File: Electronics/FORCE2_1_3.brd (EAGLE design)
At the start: 148.7 x 33.1 mm, 17 parts, among them J4 PTH, SW1 22-23-2031, SW2 22-23-2031, X1 22-23-2051, X2 22-23-2051, X3 22-23-2021

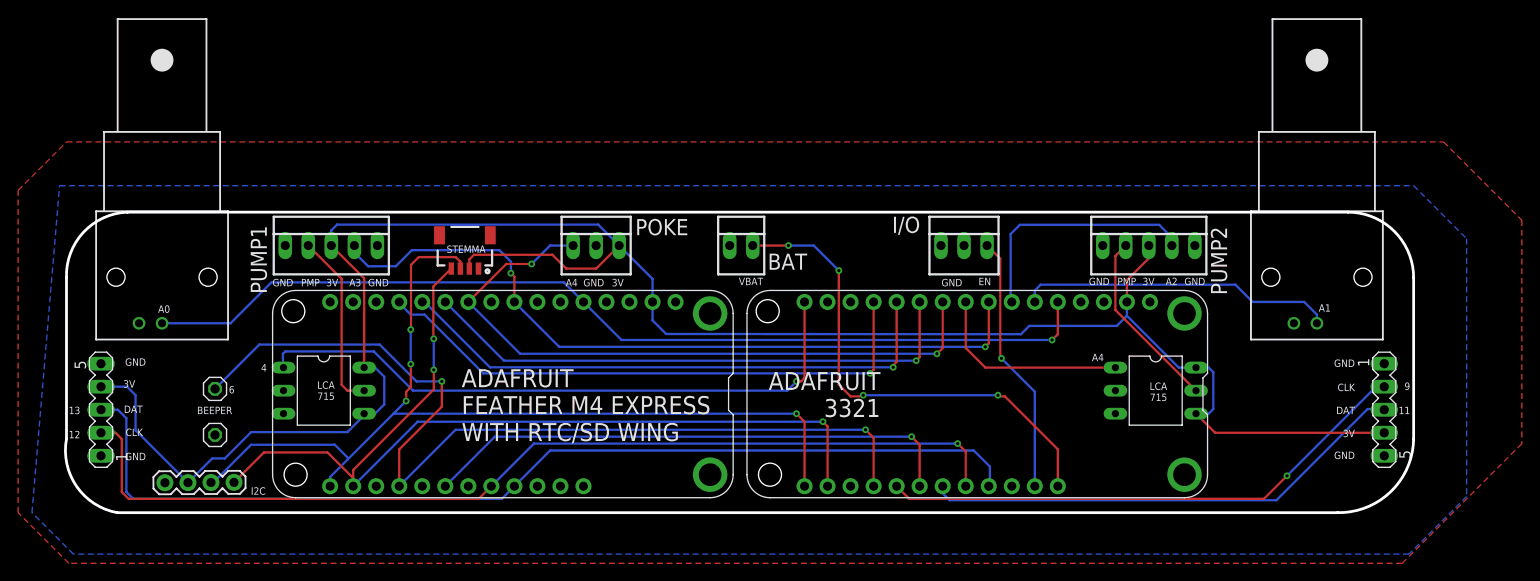
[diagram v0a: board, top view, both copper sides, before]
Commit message: First commit. Added electronics, stl file, and readme
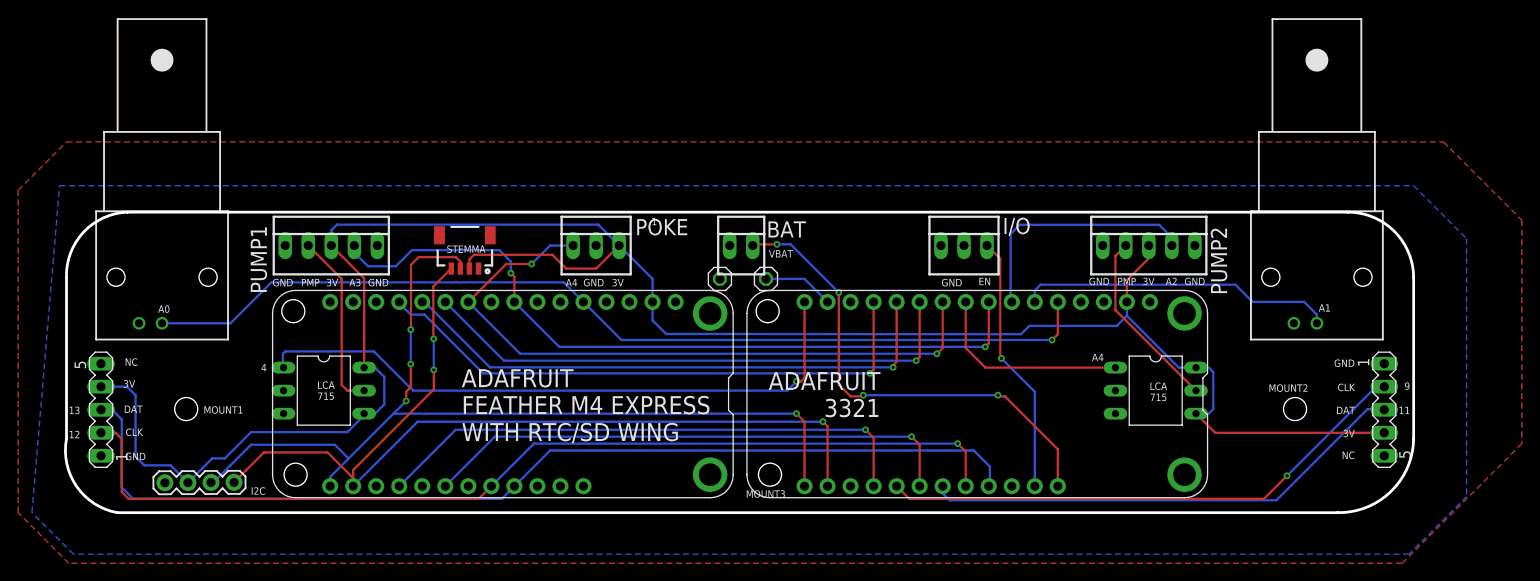
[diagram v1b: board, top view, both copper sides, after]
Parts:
- moved BEEP1 62.0 mm to (76.6, 27.1)
- moved GND 58.3 mm to (71.6, 27.1), turned to 270 degrees
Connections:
- net 1: now also BEEP1.1
- net 6: no longer BEEP1.1
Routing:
- net 6: track 102.8 -> 60.6 mm, vias 2 -> 1
- net 1: track 0.00 -> 7.85 mm
- net 3V: track 228.5 -> 230.2 mm
- net VBAT: track 54.5 -> 53.2 mm
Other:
- board text added: "1"
- board text added: "Designed by Alex Legaria v1.3 OCT2022"
- board text added: "MOUNT1"
- board text added: "MOUNT2"
- board text added: "MOUNT3"
- board text added: "NC"
- board text removed: "6"
- board text removed: "Designed by Alex Legaria v1.2 SEP2022"
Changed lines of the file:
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@@
 <drawing>
 <settings>
-<setting alwaysvectorfont="yes"/>
+<setting alwaysvectorfont="no"/>
 <setting verticaltext="up"/>
 </settings>
@@
 <wire x1="-0.508" y1="9.398" x2="-0.508" y2="27.178" width="0.3048" layer="20"/>
 <wire x1="-0.508" y1="27.178" x2="6.223" y2="34.417" width="0.3048" layer="20" curve="-90"/>
-<text x="76.835" y="28.067" size="1.778" layer="25">BAT</text>
-<text x="90.551" y="32.131" size="1.778" layer="25">I/O</text>
+<text x="76.708" y="31.623" size="1.778" layer="25">BAT</text>
+<text x="102.743" y="32.004" size="1.778" layer="25">I/O</text>
 <text x="62.23" y="31.877" size="1.778" layer="25">POKE</text>
 <text x="127.508" y="25.273" size="1.778" layer="25" rot="R90">PUMP2</text>
@@
 <text x="113.919" y="18.796" size="0.8128" layer="25" rot="R180">A4</text>
 <text x="7.076784375" y="15.875" size="0.8128" layer="25" rot="R180">3V</text>
-<text x="8.255" y="18.288" size="0.8128" layer="25" rot="R180">GND</text>
+<text x="7.366" y="18.288" size="0.8128" layer="25" rot="R180">NC</text>
 <text x="7.92474375" y="10.541" size="0.8128" layer="25" rot="R180">CLK</text>
 <text x="7.897965625" y="13.081" size="0.8128" layer="25" rot="R180">DAT</text>
 <text x="8.255" y="7.874" size="0.8128" layer="25" rot="R180">GND</text>
-<text x="141.605" y="8.001" size="0.8128" layer="25" rot="R180">GND</text>
+<text x="141.605" y="8.001" size="0.8128" layer="25" rot="R180">NC</text>
 <text x="21.59" y="17.653" size="0.8128" layer="25" rot="R180">4</text>
 <text x="27.432" y="27.051" size="0.8128" layer="25" rot="R180">PMP</text>
@@
 <text x="98.298" y="27.051" size="0.8128" layer="25" rot="R180">GND</text>
 <text x="101.473" y="27.178" size="0.8128" layer="25" rot="R180">EN</text>
-<text x="76.327" y="27.178" size="0.8128" layer="25" rot="R180">VBAT</text>
+<text x="79.629" y="30.226" size="0.8128" layer="25" rot="R180">VBAT</text>
 <text x="1.016" y="10.287" size="0.8128" layer="25" rot="R180">12</text>
 <text x="1.016" y="12.954" size="0.8128" layer="25" rot="R180">13</text>
@@
 <text x="29.083" y="15.748" size="0.8128" layer="25" rot="R180">LCA
 715</text>
-<text x="20.9677" y="29.4386" size="4.1148" layer="26" rot="MR0">FORCE2</text>
-<text x="92.6084" y="25.7048" size="1.4732" layer="26" rot="MR0">Designed by
+<text x="16.2687" y="30.2006" size="2.8448" layer="26" rot="MR0">FORCE2</text>
+<text x="94.1324" y="25.7048" size="1.4732" layer="26" rot="MR0">Designed by
 Alex Legaria
-v1.2 SEP2022
+v1.3 OCT2022
 </text>
-<text x="94.1324" y="25.9842" size="1.4732" layer="26" rot="MR0">www.kravitzlab.com</text>
+<text x="94.2594" y="26.3652" size="1.2192" layer="26" rot="MR0">www.kravitzlab.com</text>
 <text x="43.0784" y="9.1694" size="1.9812" layer="25">ADAFRUIT
 FEATHER M4 EXPRESS
@@
 3321
 </text>
-<text x="17.78" y="12.954" size="0.8128" layer="25" rot="R180">BEEPER</text>
-<text x="18.034" y="15.24" size="0.8128" layer="25" rot="R180">6</text>
+<text x="71.882" y="28.956" size="0.8128" layer="26" rot="MR180">BEEPER</text>
+<text x="64.643" y="33.782" size="0.8128" layer="25" rot="R180">1</text>
+<hole x="12.7" y="12.7" drill="2.54"/>
+<hole x="135.001" y="12.7" drill="2.54"/>
+<text x="14.605" y="12.192" size="0.8128" layer="25">MOUNT1</text>
+<text x="74.422" y="2.921" size="0.8128" layer="25">MOUNT3</text>
+<text x="132.08" y="14.605" size="0.8128" layer="25">MOUNT2</text>
 </plain>
 <attributes>
@@
 <attribute name="VALUE" x="141.9225" y="15.1638" size="1.27" layer="27" ratio="10" rot="R270"/>
 </element>
-<element name="BEEP1" library="pinhead" package="1X01" value="" x="15.875" y="14.9225" smashed="yes" rot="R90">
-<attribute name="VALUE" x="19.05" y="13.6525" size="1.27" layer="27" rot="R90"/>
-</element>
-<element name="GND" library="pinhead" package="1X01" value="" x="15.875" y="9.8425" smashed="yes">
-<attribute name="VALUE" x="14.605" y="6.6675" size="1.27" layer="27"/>
+<element name="BEEP1" library="pinhead" package="1X01" value="" x="76.6445" y="27.051" smashed="yes" rot="R90">
+<attribute name="VALUE" x="79.8195" y="25.781" size="1.27" layer="27" rot="R90"/>
+</element>
+<element name="GND" library="pinhead" package="1X01" value="" x="71.5645" y="27.051" smashed="yes" rot="R270">
+<attribute name="VALUE" x="68.3895" y="28.321" size="1.27" layer="27" rot="R270"/>
 </element>
 <element name="SW1" library="con-molex" library_urn="urn:adsk.eagle:library:165" package="22-23-2031" package3d_urn="urn:adsk.eagle:package:8078634/1" value="22-23-2031" x="98.4885" y="30.734" smashed="yes">
@@
 <contactref element="MS1" pad="2"/>
 <contactref element="MS2" pad="2"/>
-<wire x1="12.8904625" y1="4.585296875" x2="7.112" y2="10.363759375" width="0.254" layer="16"/>
-<wire x1="7.112" y1="10.363759375" x2="7.112" y2="14.224" width="0.254" layer="16"/>
+<wire x1="12.8904625" y1="4.585296875" x2="10.9854625" y2="6.490296875" width="0.254" layer="16"/>
+<wire x1="10.9854625" y1="6.490296875" x2="8.0644625" y2="6.490296875" width="0.254" layer="16"/>
+<wire x1="8.0644625" y1="6.490296875" x2="7.112" y2="7.442759375" width="0.254" layer="16"/>
+<wire x1="7.112" y1="7.442759375" x2="7.112" y2="14.224" width="0.254" layer="16"/>
 <wire x1="7.112" y1="14.224" x2="6.1722" y2="15.1638" width="0.254" layer="16"/>
 <wire x1="6.1722" y1="15.1638" x2="3.302" y2="15.1638" width="0.254" layer="16"/>
@@
 <signal name="1">
 <contactref element="MS2" pad="15"/>
+<contactref element="BEEP1" pad="1"/>
+<wire x1="80.899" y1="27.051" x2="83.439" y2="24.511" width="0.254" layer="16"/>
+<wire x1="76.6445" y1="27.051" x2="80.899" y2="27.051" width="0.254" layer="16"/>
 </signal>
 <signal name="4">
@@
 </signal>
 <signal name="6">
-<contactref element="BEEP1" pad="1"/>
 <contactref element="MS2" pad="20"/>
 <contactref element="MS1" pad="20"/>
@@
 <wire x1="87.63" y1="10.414" x2="42.417996875" y2="10.414" width="0.254" layer="16"/>
 <wire x1="42.417996875" y1="10.414" x2="36.195" y2="4.191003125" width="0.254" layer="16"/>
-<wire x1="36.195" y1="4.191003125" x2="36.195" y2="8.255" width="0.254" layer="1"/>
-<wire x1="36.195" y1="8.255" x2="40.894" y2="12.954" width="0.254" layer="1"/>
-<wire x1="40.894" y1="12.954" x2="40.894" y2="15.748" width="0.254" layer="1"/>
-<via x="40.894" y="15.748" extent="1-16" drill="0.35"/>
-<wire x1="40.894" y1="15.748" x2="38.1" y2="15.748" width="0.254" layer="16"/>
-<wire x1="38.1" y1="15.748" x2="34.036" y2="19.812" width="0.254" layer="16"/>
-<wire x1="34.036" y1="19.812" x2="20.7645" y2="19.812" width="0.254" layer="16"/>
-<wire x1="20.7645" y1="19.812" x2="15.875" y2="14.9225" width="0.254" layer="16"/>
 </signal>
 <signal name="9">
@@
 <wire x1="48.895" y1="4.191003125" x2="47.497996875" y2="2.794" width="0.254" layer="16"/>
 <wire x1="47.497996875" y1="2.794" x2="6.858" y2="2.794" width="0.254" layer="16"/>
-<wire x1="6.858" y1="2.794" x2="6.096" y2="3.556" width="0.254" layer="16"/>
-<wire x1="6.096" y1="3.556" x2="6.096" y2="11.684" width="0.254" layer="16"/>
-<wire x1="6.096" y1="11.684" x2="5.1562" y2="12.6238" width="0.254" layer="16"/>
-<wire x1="5.1562" y1="12.6238" x2="3.302" y2="12.6238" width="0.254" layer="16"/>
+<wire x1="6.858" y1="2.794" x2="5.588" y2="4.064" width="0.254" layer="16"/>
+<wire x1="5.588" y1="4.064" x2="5.588" y2="11.557" width="0.254" layer="16"/>
+<wire x1="5.588" y1="11.557" x2="4.5212" y2="12.6238" width="0.254" layer="16"/>
+<wire x1="4.5212" y1="12.6238" x2="3.302" y2="12.6238" width="0.254" layer="16"/>
 </signal>
 <signal name="USB">
@@
 <contactref element="MS2" pad="28"/>
 <contactref element="X3" pad="2"/>
-<wire x1="84.6836" y1="27.9654" x2="84.6836" y2="15.3924" width="0.254" layer="1"/>
+<wire x1="84.6836" y1="25.5524" x2="84.6836" y2="15.3924" width="0.254" layer="1"/>
 <wire x1="84.6836" y1="15.3924" x2="85.979" y2="14.097" width="0.254" layer="1"/>
 <wire x1="102.997" y1="14.097" x2="108.839" y2="8.255" width="0.254" layer="1"/>
 <wire x1="108.839" y1="8.255" x2="108.839" y2="4.191" width="0.254" layer="1"/>
-<wire x1="75.184" y1="30.734" x2="79.121" y2="30.734" width="0.254" layer="1"/>
-<via x="79.121" y="30.734" extent="1-16" drill="0.35"/>
-<wire x1="79.121" y1="30.734" x2="81.915" y2="30.734" width="0.254" layer="16"/>
-<wire x1="81.915" y1="30.734" x2="84.6836" y2="27.9654" width="0.254" layer="16"/>
-<via x="84.6836" y="27.9654" extent="1-16" drill="0.35"/>
+<wire x1="77.851" y1="30.861" x2="75.311" y2="30.861" width="0.254" layer="1"/>
+<wire x1="75.184" y1="30.734" x2="75.311" y2="30.861" width="0.254" layer="1"/>
+<via x="77.851" y="30.861" extent="1-16" drill="0.35"/>
+<wire x1="77.851" y1="30.861" x2="79.375" y2="30.861" width="0.254" layer="16"/>
+<wire x1="79.375" y1="30.861" x2="84.6836" y2="25.5524" width="0.254" layer="16"/>
+<via x="84.6836" y="25.5524" extent="1-16" drill="0.35"/>
 <wire x1="85.979" y1="14.097" x2="87.249" y2="14.097" width="0.254" layer="1"/>
 <wire x1="87.249" y1="14.097" x2="87.376" y2="14.224" width="0.254" layer="1"/>
